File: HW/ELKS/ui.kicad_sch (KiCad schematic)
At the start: 30 parts, among them Q1 Q_NMOS_GSD, SW1 SW, SW2 SW, SW3 SW

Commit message: Kikit JLC export
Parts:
- BZ1: LCSC (none) -> C201041
- Q1: JLCPCB_CORRECTION (none) -> 0;0;180
- R1, R2, R3: LCSC (none) -> C22828
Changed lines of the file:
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@@
+      (effects (font (size 1.27 1.27)) hide)
+    )
+    (property "LCSC" "C22828" (id 4) (at 55.88 52.07 0)
       (effects (font (size 1.27 1.27)) hide)
     )
@@
     )
     (property "Datasheet" "~" (id 3) (at 234.315 124.46 90)
+      (effects (font (size 1.27 1.27)) hide)
+    )
+    (property "LCSC" "C201041" (id 4) (at 234.95 127 0)
       (effects (font (size 1.27 1.27)) hide)
     )
@@
       (effects (font (size 1.27 1.27)) hide)
     )
+    (property "LCSC" "C22828" (id 4) (at 55.88 90.17 0)
+      (effects (font (size 1.27 1.27)) hide)
+    )
     (pin "1")
     (pin "2")
@@
       (effects (font (size 1.27 1.27)) hide)
     )
+    (property "LCSC" "C22828" (id 4) (at 55.88 128.27 0)
+      (effects (font (size 1.27 1.27)) hide)
+    )
     (pin "1")
     (pin "2")
@@
       (effects (font (size 1.27 1.27)) hide)
     )
+    (property "JLCPCB_CORRECTION" "0;0;180" (id 5) (at 220.98 137.16 0)
+      (effects (font (size 1.27 1.27)) hide)
+    )

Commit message: Fix potentiometers footprints and relocation two component
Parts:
- BZ1: LCSC C201041 -> (none)
- Q1: JLCPCB_CORRECTION 0;0;180 -> (none)
- R1, R2, R3: LCSC C22828 -> (none)
- RV1, RV2: footprint Potentiometer_THT:Potentiometer_Alpha_RD901F-40-00D_Single_Vertical -> Robotarna_KiCad_Library:RK09K113 (ELKS-POT)
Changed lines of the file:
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@@
-      (effects (font (size 1.27 1.27)) hide)
-    )
-    (property "LCSC" "C22828" (id 4) (at 55.88 52.07 0)
       (effects (font (size 1.27 1.27)) hide)
     )
@@
     )
     (property "Datasheet" "~" (id 3) (at 234.315 124.46 90)
-      (effects (font (size 1.27 1.27)) hide)
-    )
-    (property "LCSC" "C201041" (id 4) (at 234.95 127 0)
       (effects (font (size 1.27 1.27)) hide)
     )
@@
       (effects (font (size 1.27 1.27)) hide)
     )
-    (property "LCSC" "C22828" (id 4) (at 55.88 90.17 0)
-      (effects (font (size 1.27 1.27)) hide)
-    )
     (pin "1")
     (pin "2")
@@
       (effects (font (size 1.27 1.27)) hide)
     )
-    (property "LCSC" "C22828" (id 4) (at 55.88 128.27 0)
-      (effects (font (size 1.27 1.27)) hide)
-    )
     (pin "1")
     (pin "2")
@@
       (effects (font (size 1.27 1.27)) (justify right))
     )
-    (property "Footprint" "Potentiometer_THT:Potentiometer_Alpha_RD901F-40-00D_Single_Vertical" (id 2) (at 139.7 92.71 0)
+    (property "Footprint" "Robotarna_KiCad_Library:RK09K113 (ELKS-POT)" (id 2) (at 139.7 92.71 0)
       (effects (font (size 1.27 1.27)) hide)
     )
@@
       (effects (font (size 1.27 1.27)) (justify right))
     )
-    (property "Footprint" "Potentiometer_THT:Potentiometer_Alpha_RD901F-40-00D_Single_Vertical" (id 2) (at 139.7 130.81 0)
+    (property "Footprint" "Robotarna_KiCad_Library:RK09K113 (ELKS-POT)" (id 2) (at 139.7 130.81 0)
       (effects (font (size 1.27 1.27)) hide)
     )
@@
       (effects (font (size 1.27 1.27)) hide)
     )
-    (property "JLCPCB_CORRECTION" "0;0;180" (id 5) (at 220.98 137.16 0)
-      (effects (font (size 1.27 1.27)) hide)
-    )

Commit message: Levelshifter fix
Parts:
- R1, R11, R13, R2, R3, R7, R8: footprint Capacitor_SMD:C_0603_1608Metric -> Resistor_SMD:R_0603_1608Metric
- R4, R5, R6: footprint Capacitor_SMD:C_0402_1005Metric -> Resistor_SMD:R_0402_1005Metric
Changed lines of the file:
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@@
     (property "Reference" "R1" (id 0) (at 55.88 45.72 90))
     (property "Value" "180" (id 1) (at 55.88 48.26 90))
-    (property "Footprint" "Capacitor_SMD:C_0603_1608Metric" (id 2) (at 55.88 53.848 90)
+    (property "Footprint" "Resistor_SMD:R_0603_1608Metric" (id 2) (at 55.88 53.848 90)
       (effects (font (size 1.27 1.27)) hide)
     )
@@
       (effects (font (size 1.27 1.27)) (justify left))
     )
-    (property "Footprint" "Capacitor_SMD:C_0402_1005Metric" (id 2) (at 74.422 45.72 90)
+    (property "Footprint" "Resistor_SMD:R_0402_1005Metric" (id 2) (at 74.422 45.72 90)
       (effects (font (size 1.27 1.27)) hide)
     )
@@
     (property "Reference" "R7" (id 0) (at 120.65 86.36 90))
     (property "Value" "180" (id 1) (at 120.65 88.9 90))
-    (property "Footprint" "Capacitor_SMD:C_0603_1608Metric" (id 2) (at 120.65 94.488 90)
+    (property "Footprint" "Resistor_SMD:R_0603_1608Metric" (id 2) (at 120.65 94.488 90)
       (effects (font (size 1.27 1.27)) hide)
     )
@@
     (property "Reference" "R2" (id 0) (at 55.88 83.82 90))
     (property "Value" "180" (id 1) (at 55.88 86.36 90))
-    (property "Footprint" "Capacitor_SMD:C_0603_1608Metric" (id 2) (at 55.88 91.948 90)
+    (property "Footprint" "Resistor_SMD:R_0603_1608Metric" (id 2) (at 55.88 91.948 90)
       (effects (font (size 1.27 1.27)) hide)
     )
@@
     (property "Reference" "R8" (id 0) (at 120.65 124.46 90))
     (property "Value" "180" (id 1) (at 120.65 127 90))
-    (property "Footprint" "Capacitor_SMD:C_0603_1608Metric" (id 2) (at 120.65 132.588 90)
+    (property "Footprint" "Resistor_SMD:R_0603_1608Metric" (id 2) (at 120.65 132.588 90)
       (effects (font (size 1.27 1.27)) hide)
     )
@@
     (property "Reference" "R3" (id 0) (at 55.88 121.92 90))
     (property "Value" "180" (id 1) (at 55.88 124.46 90))
-    (property "Footprint" "Capacitor_SMD:C_0603_1608Metric" (id 2) (at 55.88 130.048 90)
+    (property "Footprint" "Resistor_SMD:R_0603_1608Metric" (id 2) (at 55.88 130.048 90)
       (effects (font (size 1.27 1.27)) hide)
     )
@@
       (effects (font (size 1.27 1.27)) (justify left))
     )
-    (property "Footprint" "Capacitor_SMD:C_0402_1005Metric" (id 2) (at 74.422 121.92 90)
+    (property "Footprint" "Resistor_SMD:R_0402_1005Metric" (id 2) (at 74.422 121.92 90)
       (effects (font (size 1.27 1.27)) hide)
     )
@@
       (effects (font (size 1.27 1.27)) (justify right))
     )
-    (property "Footprint" "Capacitor_SMD:C_0603_1608Metric" (id 2) (at 225.298 118.11 90)
+    (property "Footprint" "Resistor_SMD:R_0603_1608Metric" (id 2) (at 225.298 118.11 90)
       (effects (font (size 1.27 1.27)) hide)
     )
@@
       (effects (font (size 1.27 1.27)) (justify left))
     )
-    (property "Footprint" "Capacitor_SMD:C_0402_1005Metric" (id 2) (at 74.422 83.82 90)
+    (property "Footprint" "Resistor_SMD:R_0402_1005Metric" (id 2) (at 74.422 83.82 90)
       (effects (font (size 1.27 1.27)) hide)
     )
@@
     (property "Reference" "R11" (id 0) (at 205.74 139.7 90))
     (property "Value" "180" (id 1) (at 212.09 139.7 90))
-    (property "Footprint" "Capacitor_SMD:C_0603_1608Metric" (id 2) (at 209.55 135.382 90)
-      (effects (font (size 1.27 1.27)) hide)
-    )
+    (property "Footprint" "Resistor_SMD:R_0603_1608Metric" (id 2) (at 209.55 135.382 90)
+      (effects (font (size 1.27 1.27)) hide)
+    )

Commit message: USB shift
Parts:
- BZ1: LCSC (none) -> C201041
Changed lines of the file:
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@@
+      (effects (font (size 1.27 1.27)) hide)
+    )
+    (property "LCSC" "C201041" (id 4) (at 234.95 127 0)
       (effects (font (size 1.27 1.27)) hide)
     )

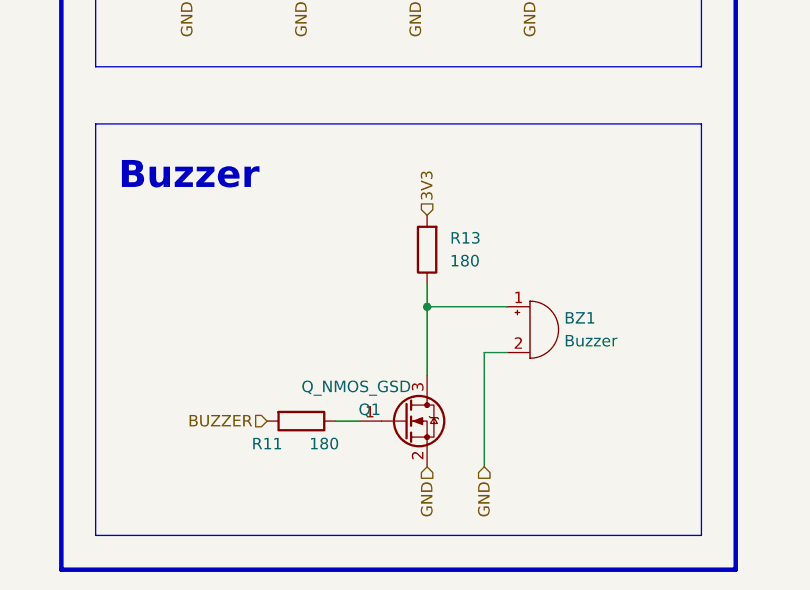
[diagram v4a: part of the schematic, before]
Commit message: Buzzer connected directly to ESP, UES diodes
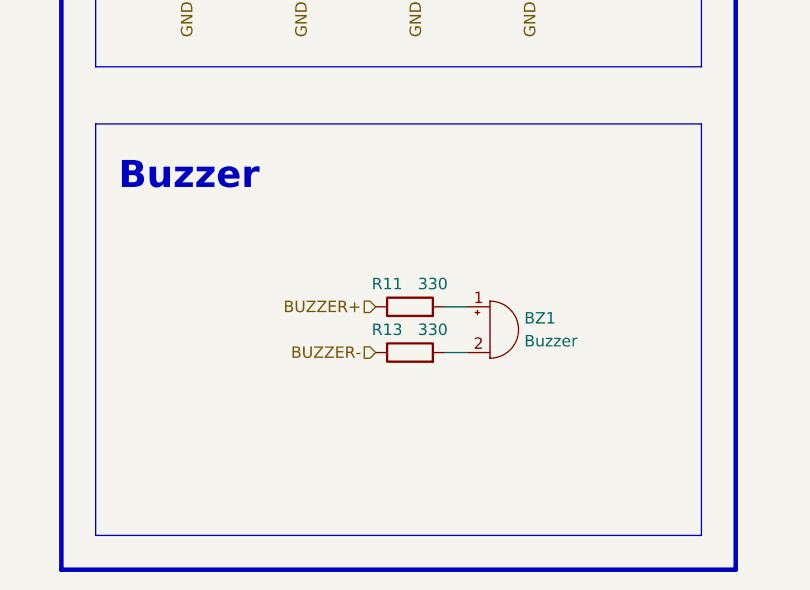
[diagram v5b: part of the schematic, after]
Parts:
- removed Q1: Q_NMOS_GSD, Package_TO_SOT_SMD:SOT-23, symbol Device:Q_NMOS_GSD
- R1, R2, R3: LCSC (none) -> C22828
- R11, R13: value 180 -> 330; footprint Resistor_SMD:R_0603_1608Metric -> Resistor_SMD:R_0402_1005Metric; LCSC C22828 -> C25104
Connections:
- net BUZZER is gone; now on an unnamed net: R11.2
- net 3V3: no longer R13.2
- net GND: no longer BZ1.2 (+)
- net at BZ1.1 (-): no longer R13.1
- net BUZZER+: now reaches R11.1
- new net: BZ1.2 (+), R13.2
- new net BUZZER-: R13.1
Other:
- moved on the sheet: BZ1
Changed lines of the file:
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@@
   (junction (at 62.23 52.07) (diameter 0) (color 0 0 0 0)
   )
-  (junction (at 223.52 124.46) (diameter 0) (color 0 0 0 0)
-  )
   (junction (at 73.66 128.27) (diameter 0) (color 0 0 0 0)
   )
@@
   (junction (at 76.2 90.17) (diameter 0) (color 0 0 0 0)
   )
-  (wire (pts (xy 229.87 129.54) (xy 232.41 129.54))
-    (stroke (width 0) (type default) (color 0 0 0 0))
-  )
   (polyline (pts (xy 254 149.86) (xy 254 104.14))
     (stroke (width 0) (type default) (color 0 0 0 0))
@@
     (stroke (width 0) (type default) (color 0 0 0 0))
   )
-  (wire (pts (xy 223.52 132.08) (xy 223.52 124.46))
-    (stroke (width 0) (type default) (color 0 0 0 0))
-  )
   (wire (pts (xy 73.66 90.17) (xy 76.2 90.17))
     (stroke (width 0) (type default) (color 0 0 0 0))
   )
   (wire (pts (xy 73.66 128.27) (xy 73.66 130.81))
+    (stroke (width 0) (type default) (color 0 0 0 0))
+  )
+  (wire (pts (xy 225.425 129.54) (xy 227.965 129.54))
     (stroke (width 0) (type default) (color 0 0 0 0))
   )
@@
     (stroke (width 0.5) (type solid) (color 0 0 0 0))
   )
-  (wire (pts (xy 223.52 124.46) (xy 232.41 124.46))
-    (stroke (width 0) (type default) (color 0 0 0 0))
-  )
   (wire (pts (xy 124.46 130.81) (xy 127 130.81))
     (stroke (width 0) (type default) (color 0 0 0 0))
   )
-  (wire (pts (xy 223.52 121.92) (xy 223.52 124.46))
-    (stroke (width 0) (type default) (color 0 0 0 0))
-  )
   (wire (pts (xy 127 92.71) (xy 135.89 92.71))
     (stroke (width 0) (type default) (color 0 0 0 0))
@@
   )
   (wire (pts (xy 62.23 130.81) (xy 62.23 128.27))
-    (stroke (width 0) (type default) (color 0 0 0 0))
-  )
-  (wire (pts (xy 229.87 142.24) (xy 229.87 129.54))
     (stroke (width 0) (type default) (color 0 0 0 0))
   )
@@
     (stroke (width 0) (type default) (color 0 0 0 0))
   )
-  (wire (pts (xy 213.36 137.16) (xy 215.9 137.16))
+  (wire (pts (xy 225.425 124.46) (xy 227.965 124.46))
     (stroke (width 0) (type default) (color 0 0 0 0))
   )
@@
     (effects (font (size 1.27 1.27)) (justify right))
   )
+  (hierarchical_label "BUZZER-" (shape input) (at 217.805 129.54 180)
+    (effects (font (size 1.27 1.27)) (justify right))
+  )
   (hierarchical_label "GND" (shape input) (at 127 140.97 270)
     (effects (font (size 1.27 1.27)) (justify right))
@@
     (effects (font (size 1.27 1.27)) (justify right))
   )
-  (hierarchical_label "BUZZER" (shape input) (at 205.74 137.16 180)
+  (hierarchical_label "BUZZER+" (shape input) (at 217.805 124.46 180)
     (effects (font (size 1.27 1.27)) (justify right))
   )
@@
     (effects (font (size 1.27 1.27)) (justify left))
   )
-  (hierarchical_label "GND" (shape input) (at 223.52 142.24 270)
-    (effects (font (size 1.27 1.27)) (justify right))
-  )
-  (hierarchical_label "GND" (shape input) (at 229.87 142.24 270)
-    (effects (font (size 1.27 1.27)) (justify right))
-  )
   (hierarchical_label "3V3" (shape input) (at 76.2 118.11 90)
     (effects (font (size 1.27 1.27)) (justify left))
@@
   (hierarchical_label "POT0" (shape input) (at 116.84 92.71 180)
     (effects (font (size 1.27 1.27)) (justify right))
-  )
-  (hierarchical_label "3V3" (shape input) (at 223.52 114.3 90)
-    (effects (font (size 1.27 1.27)) (justify left))
   )
   (hierarchical_label "3V3" (shape input) (at 76.2 80.01 90)
@@
       (effects (font (size 1.27 1.27)) hide)
     )
+    (property "LCSC" "C22828" (id 4) (at 55.88 52.07 0)
+      (effects (font (size 1.27 1.27)) hide)
+    )
     (pin "1")
     (pin "2")
@@
     (pin "2")
   )
-  (symbol (lib_id "Device:Buzzer") (at 234.95 127 0) (unit 1)
-    (in_bom yes) (on_board yes) (fields_autoplaced)
-    (property "Reference" "BZ1" (id 0) (at 238.76 125.7299 0)
-      (effects (font (size 1.27 1.27)) (justify left))
-    )
-    (property "Value" "Buzzer" (id 1) (at 238.76 128.2699 0)
-      (effects (font (size 1.27 1.27)) (justify left))
-    )
-    (property "Footprint" "Robotarna_KiCad_Library:ELKS-PIEZO" (id 2) (at 234.315 124.46 90)
-      (effects (font (size 1.27 1.27)) hide)
-    )
-    (property "Datasheet" "~" (id 3) (at 234.315 124.46 90)
-      (effects (font (size 1.27 1.27)) hide)
-    )
-    (property "LCSC" "C201041" (id 4) (at 234.95 127 0)
+  (symbol (lib_id "Device:Buzzer") (at 230.505 127 0) (unit 1)
+    (in_bom yes) (on_board yes) (fields_autoplaced)
+    (property "Reference" "BZ1" (id 0) (at 234.315 125.7299 0)
+      (effects (font (size 1.27 1.27)) (justify left))
+    )
+    (property "Value" "Buzzer" (id 1) (at 234.315 128.2699 0)
+      (effects (font (size 1.27 1.27)) (justify left))
+    )
+    (property "Footprint" "Robotarna_KiCad_Library:ELKS-PIEZO" (id 2) (at 229.87 124.46 90)
+      (effects (font (size 1.27 1.27)) hide)
+    )
+    (property "Datasheet" "~" (id 3) (at 229.87 124.46 90)
+      (effects (font (size 1.27 1.27)) hide)
+    )
+    (property "LCSC" "C201041" (id 4) (at 230.505 127 0)
       (effects (font (size 1.27 1.27)) hide)
     )
@@
       (effects (font (size 1.27 1.27)) hide)
     )
+    (property "LCSC" "C22828" (id 4) (at 55.88 90.17 0)
+      (effects (font (size 1.27 1.27)) hide)
+    )
     (pin "1")
     (pin "2")
@@
       (effects (font (size 1.27 1.27)) hide)
     )
+    (property "LCSC" "C22828" (id 4) (at 55.88 128.27 0)
+      (effects (font (size 1.27 1.27)) hide)
+    )
+    (pin "1")
+    (pin "2")
+  )
+  (symbol (lib_id "Device:R") (at 221.615 124.46 90) (unit 1)
+    (in_bom yes) (on_board yes)
+    (property "Reference" "R11" (id 0) (at 219.075 121.92 90))
+    (property "Value" "330" (id 1) (at 224.155 121.92 90))
+    (property "Footprint" "Resistor_SMD:R_0402_1005Metric" (id 2) (at 221.615 126.238 90)
+      (effects (font (size 1.27 1.27)) hide)
+    )
+    (property "Datasheet" "~" (id 3) (at 221.615 124.46 0)
+      (effects (font (size 1.27 1.27)) hide)
+    )
+    (property "LCSC" "C25104" (id 4) (at 221.615 124.46 0)
+      (effects (font (size 1.27 1.27)) hide)
+    )
     (pin "1")
     (pin "2")
@@
     (pin "2")
   )
-  (symbol (lib_id "Device:R") (at 223.52 118.11 180) (unit 1)
-    (in_bom yes) (on_board yes) (fields_autoplaced)
-    (property "Reference" "R13" (id 0) (at 226.06 116.8399 0)
-      (effects (font (size 1.27 1.27)) (justify right))
-    )
-    (property "Value" "180" (id 1) (at 226.06 119.3799 0)
-      (effects (font (size 1.27 1.27)) (justify right))
-    )
-    (property "Footprint" "Resistor_SMD:R_0603_1608Metric" (id 2) (at 225.298 118.11 90)
-      (effects (font (size 1.27 1.27)) hide)
-    )
-    (property "Datasheet" "~" (id 3) (at 223.52 118.11 0)
-      (effects (font (size 1.27 1.27)) hide)
-    )
-    (property "LCSC" "C22828" (id 4) (at 223.52 118.11 90)
-      (effects (font (size 1.27 1.27)) hide)
-    )
-    (pin "1")
-    (pin "2")
-  )
   (symbol (lib_name "SW_2") (lib_id "Robotarna_KiCad_Library:SW") (at 74.93 97.79 90) (unit 1)
     (in_bom yes) (on_board yes) (fields_autoplaced)
@@
     )
     (property "LCSC" "C470311" (id 4) (at 139.7 130.81 0)
-      (effects (font (size 1.27 1.27)) hide)
-    )
-    (pin "1")
-    (pin "2")
-    (pin "3")
-  )
-  (symbol (lib_id "Device:R") (at 209.55 137.16 270) (unit 1)
-    (in_bom yes) (on_board yes)
-    (property "Reference" "R11" (id 0) (at 205.74 139.7 90))
-    (property "Value" "180" (id 1) (at 212.09 139.7 90))
-    (property "Footprint" "Resistor_SMD:R_0603_1608Metric" (id 2) (at 209.55 135.382 90)
-      (effects (font (size 1.27 1.27)) hide)
-    )
-    (property "Datasheet" "~" (id 3) (at 209.55 137.16 0)
-      (effects (font (size 1.27 1.27)) hide)
-    )
-    (property "LCSC" "C22828" (id 4) (at 209.55 137.16 90)
-      (effects (font (size 1.27 1.27)) hide)
-    )
-    (pin "1")
-    (pin "2")
-  )
-  (symbol (lib_id "Device:Q_NMOS_GSD") (at 220.98 137.16 0) (unit 1)
-    (in_bom yes) (on_board yes)
-    (property "Reference" "Q1" (id 0) (at 215.9 135.89 0)
-      (effects (font (size 1.27 1.27)) (justify left))
-    )
-    (property "Value" "Q_NMOS_GSD" (id 1) (at 209.55 133.35 0)
-      (effects (font (size 1.27 1.27)) (justify left))
-    )
-    (property "Footprint" "Package_TO_SOT_SMD:SOT-23" (id 2) (at 226.06 134.62 0)
-      (effects (font (size 1.27 1.27)) hide)
-    )
-    (property "Datasheet" "~" (id 3) (at 220.98 137.16 0)
-      (effects (font (size 1.27 1.27)) hide)
-    )
-    (property "LCSC" "C8545" (id 4) (at 220.98 137.16 0)
       (effects (font (size 1.27 1.27)) hide)
     )
@@
       (effects (font (size 1.27 1.27)) hide)
     )
+    (pin "1")
+    (pin "2")
+  )
+  (symbol (lib_id "Device:R") (at 221.615 129.54 90) (unit 1)
+    (in_bom yes) (on_board yes)
+    (property "Reference" "R13" (id 0) (at 219.075 127 90))
+    (property "Value" "330" (id 1) (at 224.155 127 90))
+    (property "Footprint" "Resistor_SMD:R_0402_1005Metric" (id 2) (at 221.615 131.318 90)
+      (effects (font (size 1.27 1.27)) hide)
+    )
+    (property "Datasheet" "~" (id 3) (at 221.615 129.54 0)
+      (effects (font (size 1.27 1.27)) hide)
+    )
+    (property "LCSC" "C25104" (id 4) (at 221.615 129.54 0)
+      (effects (font (size 1.27 1.27)) hide)
+    )

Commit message: Cleaning files
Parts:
- D3: LCSC C72043 -> C434423
